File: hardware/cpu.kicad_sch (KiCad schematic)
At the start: 16 parts, among them J1 Conn_02x02_Odd_Even, U3 ESP32-C3-WROOM-02

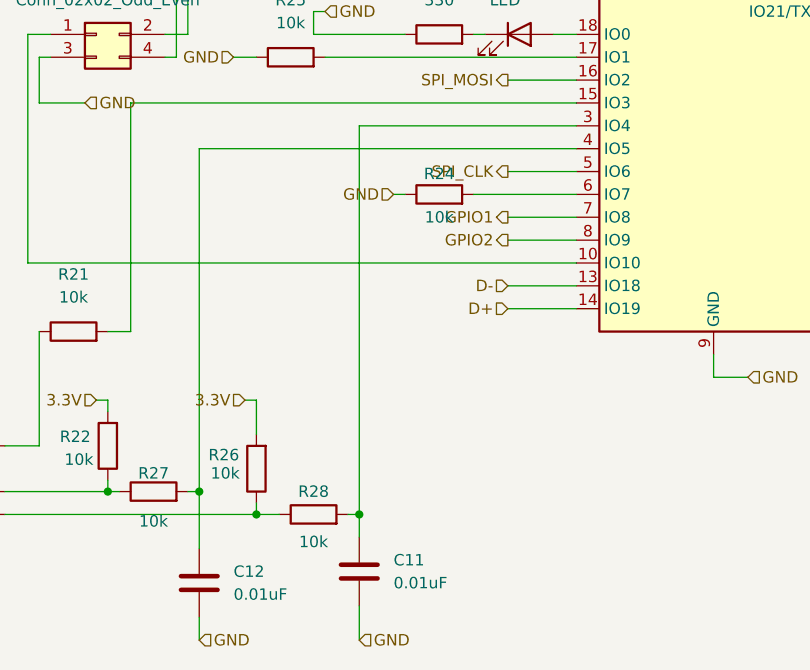
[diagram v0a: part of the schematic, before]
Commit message: Change to path on 3V3 Testpoint.
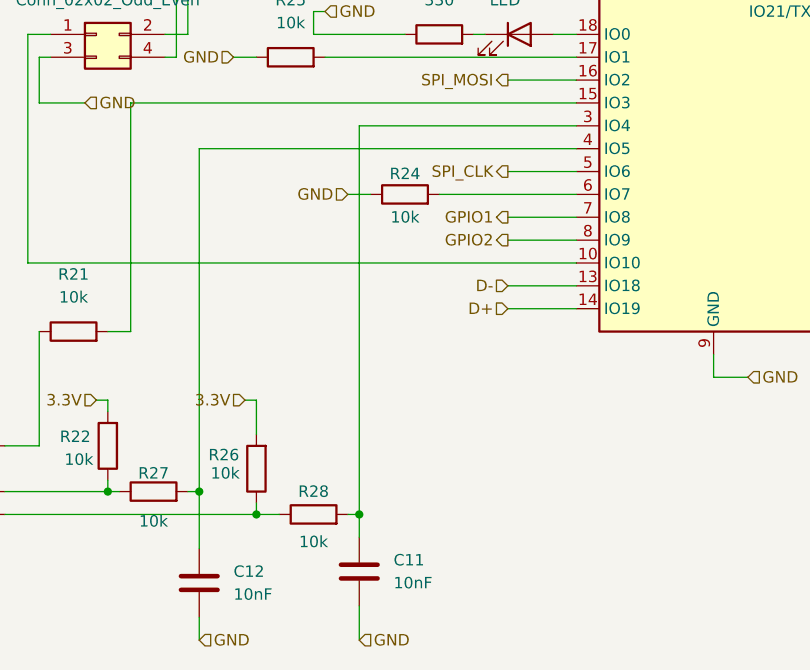
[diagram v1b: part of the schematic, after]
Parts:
- C11, C12: value 0.01uF -> 10nF
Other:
- moved on the sheet: R24
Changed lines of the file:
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@@
 	(wire
 		(pts
-			(xy 101.6 78.74) (xy 102.87 78.74)
+			(xy 96.52 78.74) (xy 99.06 78.74)
 		)
 		(stroke
@@
 	(wire
 		(pts
-			(xy 110.49 78.74) (xy 121.92 78.74)
+			(xy 106.68 78.74) (xy 121.92 78.74)
 		)
 		(stroke
@@
 	(hierarchical_label "GND"
 		(shape input)
-		(at 101.6 78.74 180)
+		(at 96.52 78.74 180)
 		(effects
 			(font
@@
 			)
 		)
-		(property "Value" "0.01uF"
+		(property "Value" "10nF"
 			(at 101.6 121.9199 0)
 			(effects
@@
 	(symbol
 		(lib_id "Device:R")
-		(at 106.68 78.74 90)
+		(at 102.87 78.74 90)
 		(unit 1)
 		(exclude_from_sim no)
@@
 		(dnp no)
 		(property "Reference" "R24"
-			(at 106.68 76.454 90)
+			(at 102.87 76.454 90)
 			(effects
 				(font
@@
 		)
 		(property "Value" "10k"
-			(at 106.68 81.28 90)
+			(at 102.87 81.28 90)
 			(effects
 				(font
@@
 		)
 		(property "Footprint" "Resistor_SMD:R_0805_2012Metric"
-			(at 106.68 80.518 90)
+			(at 102.87 80.518 90)
 			(effects
 				(font
@@
 		)
 		(property "Datasheet" "~"
-			(at 106.68 78.74 0)
+			(at 102.87 78.74 0)
 			(effects
 				(font
@@
 		)
 		(property "Description" "Resistor"
-			(at 106.68 78.74 0)
+			(at 102.87 78.74 0)
 			(effects
 				(font
@@
 			)
 		)
-		(property "Value" "0.01uF"
+		(property "Value" "10nF"
 			(at 83.82 123.1899 0)
 			(effects

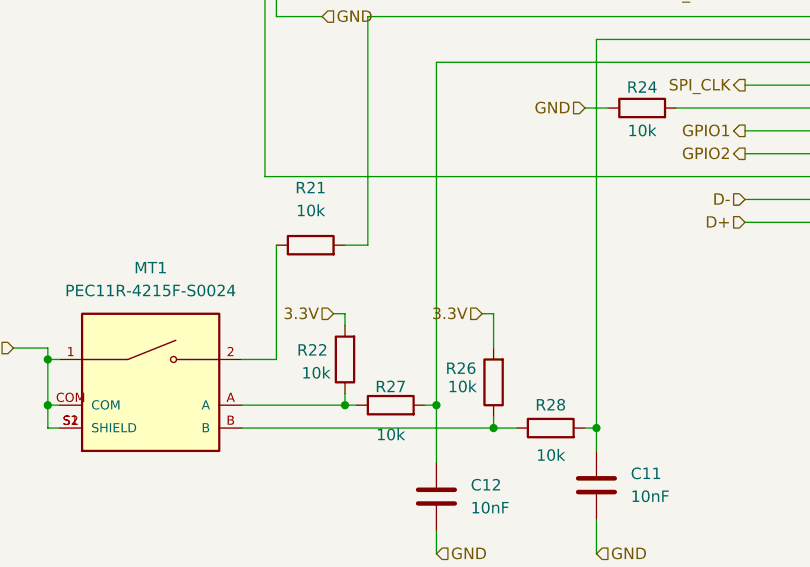
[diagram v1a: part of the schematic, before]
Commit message: Add capacitor for rotary switch.
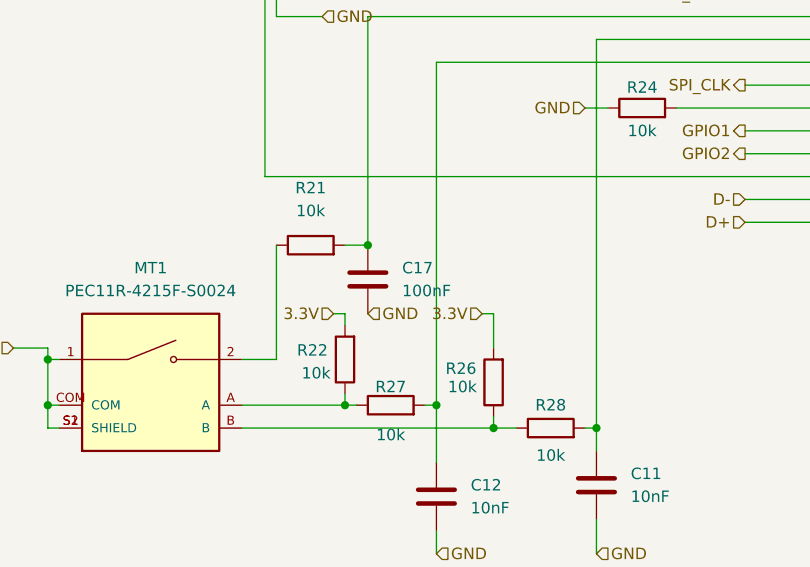
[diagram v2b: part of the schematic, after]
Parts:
- added C17: 100nF, Resistor_SMD:R_0805_2012Metric, symbol Device:C
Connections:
- net GND: now also C17.2
- net at R21.2, U3.15 (IO3): now also C17.1
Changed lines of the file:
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@@
+	)
+	(junction
+		(at 72.39 93.98)
+		(diameter 0)
+		(color 0 0 0 0)
 	)
 	(junction
@@
 			)
 			(justify right)
+		)
+	)
+	(hierarchical_label "GND"
+		(shape input)
+		(at 72.39 101.6 0)
+		(effects
+			(font
+				(size 1.27 1.27)
+			)
+			(justify left)
 		)
 	)
@@
 					(unit 1)
 				)
+			)
+		)
+	)
+	(symbol
+		(lib_id "Device:C")
+		(at 72.39 97.79 0)
+		(unit 1)
+		(exclude_from_sim no)
+		(in_bom yes)
+		(on_board yes)
+		(dnp no)
+		(fields_autoplaced yes)
+		(property "Reference" "C17"
+			(at 76.2 96.5199 0)
+			(effects
+				(font
+					(size 1.27 1.27)
+				)
+				(justify left)
+			)
+		)
+		(property "Value" "100nF"
+			(at 76.2 99.0599 0)
+			(effects
+				(font
+					(size 1.27 1.27)
+				)
+				(justify left)
+			)
+		)
+		(property "Footprint" "Resistor_SMD:R_0805_2012Metric"
+			(at 73.3552 101.6 0)
+			(effects
+				(font
+					(size 1.27 1.27)
+				)
+				(hide yes)
+			)
+		)
+		(property "Datasheet" "~"
+			(at 72.39 97.79 0)
+			(effects
+				(font
+					(size 1.27 1.27)
+				)
+				(hide yes)
+			)
+		)
+		(property "Description" "Unpolarized capacitor"
+			(at 72.39 97.79 0)
+			(effects
+				(font
+					(size 1.27 1.27)
+				)
+				(hide yes)
+			)
+		)
+		(pin "2"
+		)
+		(pin "1"
+		)
+		(instances
+			(project "nixie_clock"
+				(path "/90430e5f-7049-4de8-b92d-f897c4a89819/99bf9233-4f4b-4c20-a5a1-eeea9a6ff67a"
+					(reference "C17")
+					(unit 1)
+				)

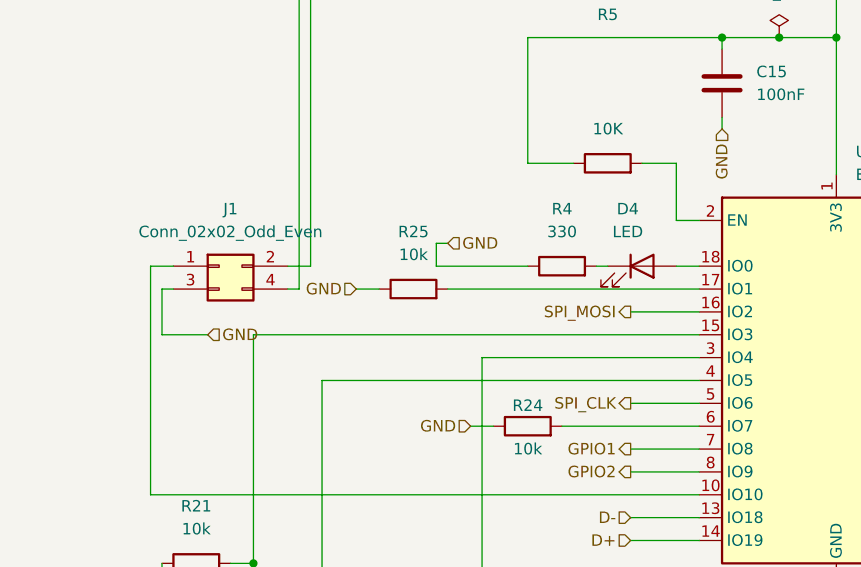
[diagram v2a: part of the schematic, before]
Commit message: Add IO1 to pin header. Add .step models.
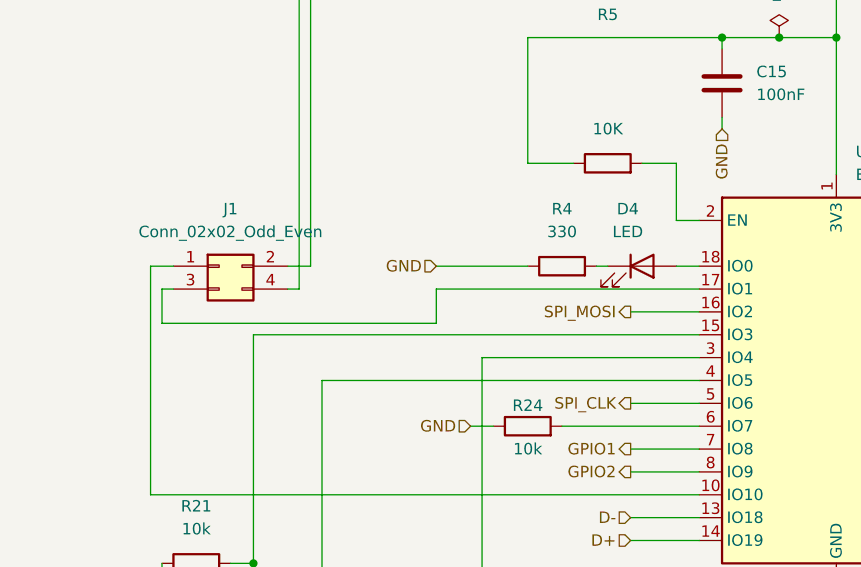
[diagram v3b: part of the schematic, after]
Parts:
- removed R25: 10k, Resistor_SMD:R_0805_2012Metric, symbol Device:R
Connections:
- net GND: no longer J1.3 (Pin_3)
- net at U3.17 (IO1): now also J1.3 (Pin_3)
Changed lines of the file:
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@@
-	(wire
-		(pts
-			(xy 93.98 63.5) (xy 121.92 63.5)
-		)
-		(stroke
-			(width 0)
-			(type default)
-		)
-	)
 	(wire
 		(pts
@@
 	(wire
 		(pts
-			(xy 92.71 58.42) (xy 93.98 58.42)
-		)
-		(stroke
-			(width 0)
-			(type default)
-		)
-	)
-	(wire
-		(pts
 			(xy 86.36 101.6) (xy 86.36 105.41)
 		)
@@
 	(wire
 		(pts
+			(xy 92.71 67.31) (xy 62.23 67.31)
+		)
+		(stroke
+			(width 0)
+			(type default)
+		)
+	)
+	(wire
+		(pts
 			(xy 80.01 73.66) (xy 121.92 73.66)
 		)
@@
 	(wire
 		(pts
+			(xy 92.71 63.5) (xy 92.71 67.31)
+		)
+		(stroke
+			(width 0)
+			(type default)
+		)
+	)
+	(wire
+		(pts
 			(xy 114.3 66.04) (xy 121.92 66.04)
 		)
@@
 	(wire
 		(pts
+			(xy 62.23 67.31) (xy 62.23 63.5)
+		)
+		(stroke
+			(width 0)
+			(type default)
+		)
+	)
+	(wire
+		(pts
 			(xy 62.23 63.5) (xy 63.5 63.5)
 		)
@@
 	(wire
 		(pts
-			(xy 92.71 58.42) (xy 92.71 60.96)
-		)
-		(stroke
-			(width 0)
-			(type default)
-		)
-	)
-	(wire
-		(pts
 			(xy 137.16 96.52) (xy 137.16 99.06)
 		)
@@
 	(wire
 		(pts
-			(xy 83.82 63.5) (xy 86.36 63.5)
-		)
-		(stroke
-			(width 0)
-			(type default)
-		)
-	)
-	(wire
-		(pts
-			(xy 62.23 68.58) (xy 62.23 63.5)
-		)
-		(stroke
-			(width 0)
-			(type default)
-		)
-	)
-	(wire
-		(pts
 			(xy 130.81 35.56) (xy 137.16 35.56)
 		)
@@
 	(wire
 		(pts
-			(xy 62.23 68.58) (xy 67.31 68.58)
-		)
-		(stroke
-			(width 0)
-			(type default)
-		)
-	)
-	(wire
-		(pts
 			(xy 119.38 60.96) (xy 121.92 60.96)
 		)
@@
 		(pts
 			(xy 80.01 111.76) (xy 80.01 118.11)
+		)
+		(stroke
+			(width 0)
+			(type default)
+		)
+	)
+	(wire
+		(pts
+			(xy 92.71 63.5) (xy 121.92 63.5)
 		)
 		(stroke
@@
 		)
 	)
-	(hierarchical_label "GND"
-		(shape input)
-		(at 67.31 68.58 0)
-		(effects
-			(font
-				(size 1.27 1.27)
-			)
-			(justify left)
-		)
-	)
 	(hierarchical_label "D+"
 		(shape input)
@@
 		)
 	)
-	(hierarchical_label "GND"
-		(shape input)
-		(at 93.98 58.42 0)
-		(effects
-			(font
-				(size 1.27 1.27)
-			)
-			(justify left)
-		)
-	)
 	(hierarchical_label "3.3V"
 		(shape input)
@@
 	(hierarchical_label "GND"
 		(shape input)
-		(at 83.82 63.5 180)
-		(effects
-			(font
-				(size 1.27 1.27)
-			)
-			(justify right)
-		)
-	)
-	(hierarchical_label "GND"
-		(shape input)
 		(at 72.39 101.6 0)
 		(effects
@@
 		(shape input)
 		(at 114.3 88.9 180)
+		(effects
+			(font
+				(size 1.27 1.27)
+			)
+			(justify right)
+		)
+	)
+	(hierarchical_label "GND"
+		(shape input)
+		(at 92.71 60.96 180)
 		(effects
 			(font
@@
 					(unit 1)
 				)
-			)
-		)
-	)
-	(symbol
-		(lib_id "Device:R")
-		(at 90.17 63.5 90)
-		(unit 1)
-		(exclude_from_sim no)
-		(in_bom yes)
-		(on_board yes)
-		(dnp no)
-		(fields_autoplaced yes)
-		(property "Reference" "R25"
-			(at 90.17 57.15 90)
-			(effects
-				(font
-					(size 1.27 1.27)
-				)
-			)
-		)
-		(property "Value" "10k"
-			(at 90.17 59.69 90)
-			(effects
-				(font
-					(size 1.27 1.27)
-				)
-			)
-		)
-		(property "Footprint" "Resistor_SMD:R_0805_2012Metric"
-			(at 90.17 65.278 90)
-			(effects
-				(font
-					(size 1.27 1.27)
-				)
-				(hide yes)
-			)
-		)
-		(property "Datasheet" "~"
-			(at 90.17 63.5 0)
-			(effects
-				(font
-					(size 1.27 1.27)
-				)
-				(hide yes)
-			)
-		)
-		(property "Description" "Resistor"
-			(at 90.17 63.5 0)
-			(effects
-				(font
-					(size 1.27 1.27)
-				)
-				(hide yes)
-			)
-		)
-		(pin "1"
-		)
-		(pin "2"
-		)
-		(instances
-			(project "nixie_clock"
-				(path "/90430e5f-7049-4de8-b92d-f897c4a89819/99bf9233-4f4b-4c20-a5a1-eeea9a6ff67a"
-					(reference "R25")
-					(unit 1)
-				)
